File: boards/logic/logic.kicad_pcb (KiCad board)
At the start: 2 copper layers, 49.7 x 57.8 mm, 45 parts, among them IC1 ATTINY85-S, P1 5V_IN, P2 PROG_CONN, P3 DSPLY_CONN, Q1 Q_NPN_EBC, Q2 Q_NPN_EBC, Q3 Q_NPN_EBC, Q4 Q_NPN_EBC, Q5 Q_NPN_EBC, Q6 Q_NPN_EBC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

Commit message: Route ESP8266 ground, and add top and bottom ground planes.
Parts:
- moved G1 1.30 mm to (137.2, 115.7)
- moved G2 1.22 mm to (137.5, 119.3)
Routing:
- net GND: track 13.5 -> 21.9 mm, vias 1 -> 2
- added copper zone on B.Cu, net GND
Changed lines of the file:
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@@
   (general
     (links 117)
-    (no_connects 30)
-    (area 97.104287 47.403566 203.751257 163.830001)
+    (no_connects 16)
+    (area 120.574999 88.824999 170.382001 146.760001)
     (thickness 1.6)
     (drawings 32)
-    (tracks 457)
+    (tracks 462)
     (zones 0)
     (modules 45)
@@
     (34 B.Paste user)
     (35 F.Paste user)
-    (36 B.SilkS user hide)
-    (37 F.SilkS user hide)
+    (36 B.SilkS user)
+    (37 F.SilkS user)
     (38 B.Mask user)
     (39 F.Mask user)
@@
   )
   (module te_logos:te_22mm_width (layer B.Cu)
-    (at 137.414 116.967 180)
+    (at 137.16 115.697 180)
     (fp_text reference G1 (at 0 0 180) (layer B.SilkS) hide
       (effects (font (thickness 0.3)) (justify mirror))
@@
   )
   (module te_logos:te_text_22mm_width (layer B.Cu)
-    (at 137.5156 120.4722 180)
+    (at 137.5156 119.253 180)
     (fp_text reference G2 (at 0 0 180) (layer B.SilkS) hide
       (effects (font (thickness 0.3)) (justify mirror))
@@
   (segment (start 159.385 126.111) (end 156.464 123.19) (width 0.25) (layer F.Cu) (net 1))
   (segment (start 156.464 123.19) (end 131.58324 123.19) (width 0.25) (layer F.Cu) (net 1))
+  (segment (start 167.259 108.077) (end 166.7618 108.077) (width 0.5) (layer B.Cu) (net 2))
+  (segment (start 166.7618 108.077) (end 164.0948 110.744) (width 0.5) (layer B.Cu) (net 2))
+  (segment (start 167.792 104.14) (end 167.792 107.544) (width 0.5) (layer F.Cu) (net 2))
+  (via (at 167.259 108.077) (size 0.6) (drill 0.4) (layers F.Cu B.Cu) (net 2))
+  (segment (start 167.792 107.544) (end 167.259 108.077) (width 0.5) (layer F.Cu) (net 2))
   (segment (start 126.111 139.827) (end 126.111 135.215) (width 0.5) (layer B.Cu) (net 2))
   (segment (start 126.111 135.215) (end 127.468 133.858) (width 0.5) (layer B.Cu) (net 2))
@@
       )
     )
+  )
+  (zone (net 2) (net_name GND) (layer B.Cu) (hatch edge 0.508)
+    (connect_pads (clearance 0.508))
+    (min_thickness 0.254)
+    (fill yes (arc_segments 16) (thermal_gap 0.508) (thermal_bridge_width 0.508))
+    (polygon
+      (pts
+        (xy 170.18 90.297) (xy 169.799 89.535) (xy 169.037 89.154) (xy 121.92 89.154) (xy 121.158 89.408)
+        (xy 120.777 90.043) (xy 120.777 145.415) (xy 121.158 146.177) (xy 121.92 146.558) (xy 169.164 146.558)
+        (xy 169.799 146.177) (xy 170.18 145.542)
+      )
+    )

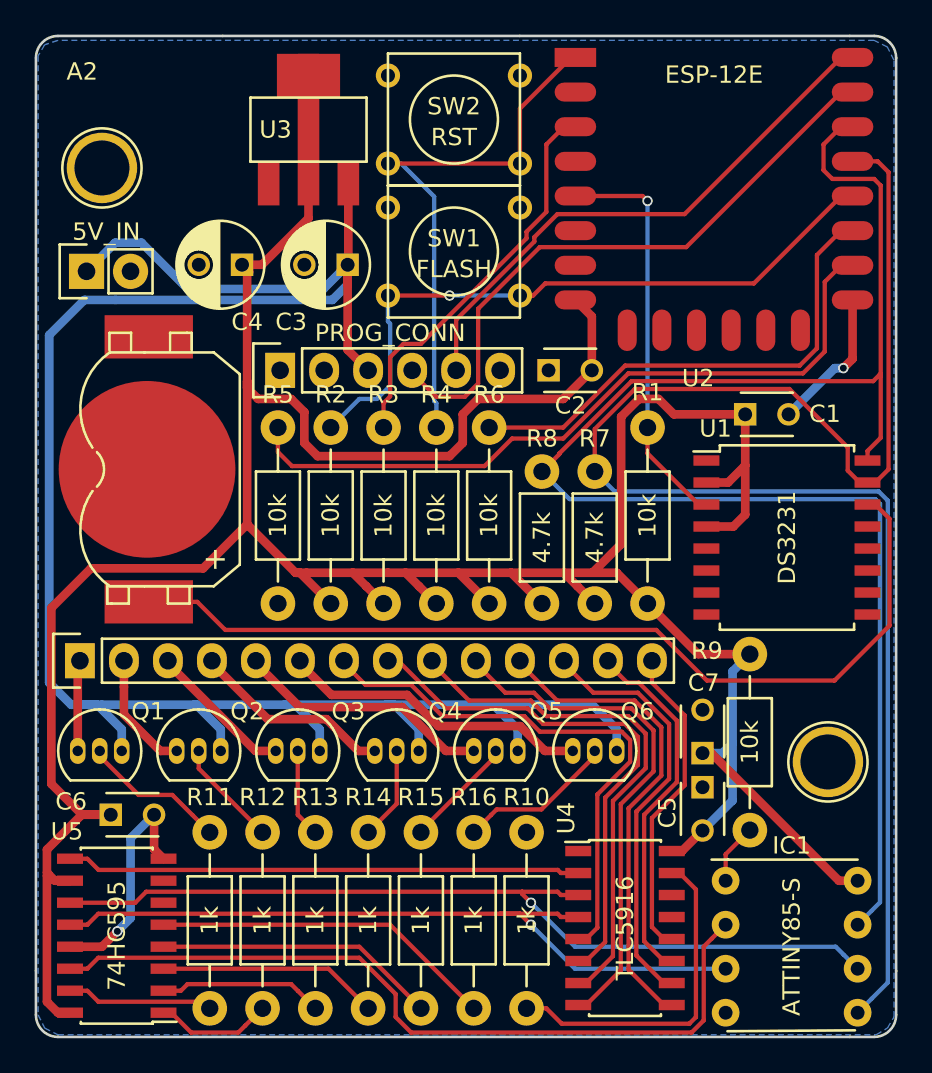
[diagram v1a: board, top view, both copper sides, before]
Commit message: Fix an unconnected ground on the TLC5916 and update the schematic date.
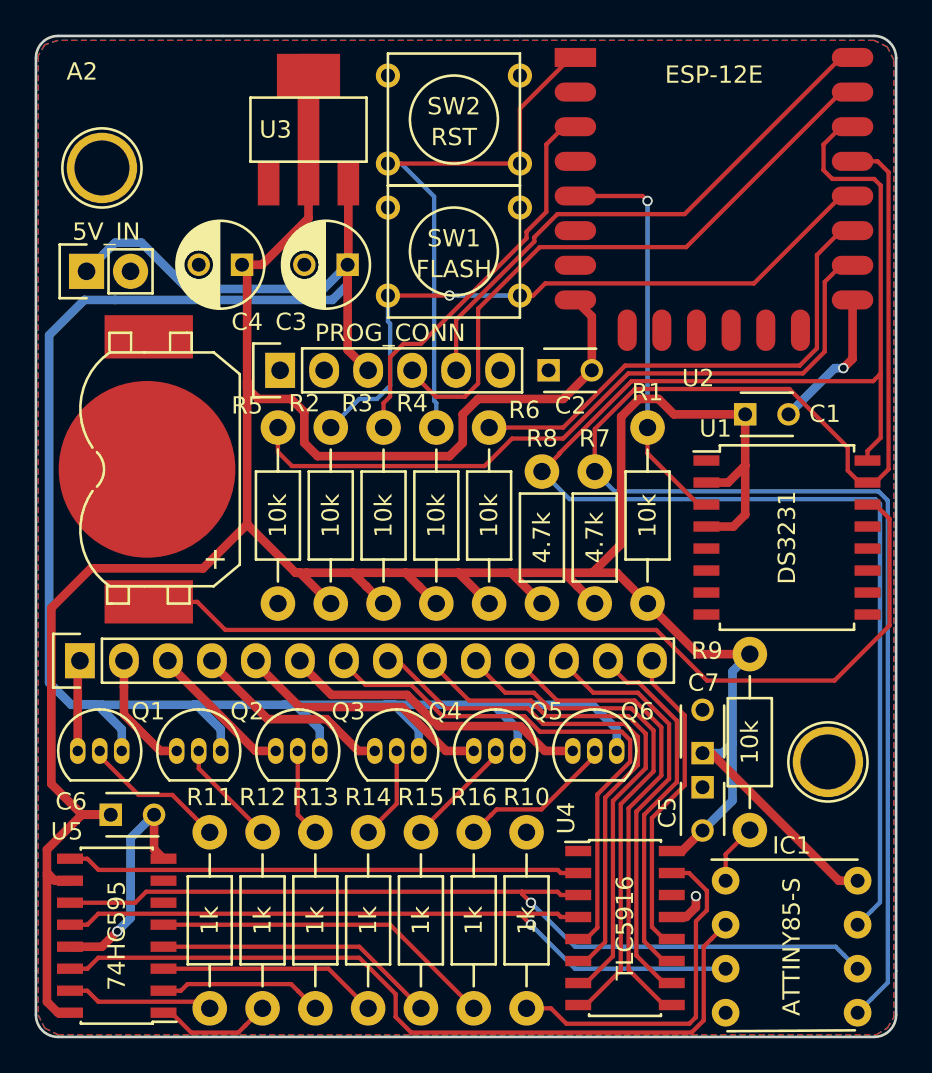
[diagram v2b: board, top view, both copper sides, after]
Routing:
- net GND: track 21.9 -> 24.2 mm, vias 2 -> 3
- net Net-(R10-Pad1): track 19.5 -> 20.3 mm
- added copper zone on F.Cu, net GND
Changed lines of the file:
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@@
   (general
     (links 117)
-    (no_connects 16)
+    (no_connects 1)
     (area 120.574999 88.824999 170.382001 146.760001)
     (thickness 1.6)
     (drawings 32)
-    (tracks 462)
+    (tracks 468)
     (zones 0)
     (modules 45)
@@
     (0 F.Cu signal)
     (31 B.Cu signal)
-    (32 B.Adhes user)
-    (33 F.Adhes user)
-    (34 B.Paste user)
-    (35 F.Paste user)
-    (36 B.SilkS user)
+    (32 B.Adhes user hide)
+    (33 F.Adhes user hide)
+    (34 B.Paste user hide)
+    (35 F.Paste user hide)
+    (36 B.SilkS user hide)
     (37 F.SilkS user)
     (38 B.Mask user)
     (39 F.Mask user)
-    (40 Dwgs.User user)
-    (41 Cmts.User user)
-    (42 Eco1.User user)
-    (43 Eco2.User user)
+    (40 Dwgs.User user hide)
+    (41 Cmts.User user hide)
+    (42 Eco1.User user hide)
+    (43 Eco2.User user hide)
     (44 Edge.Cuts user)
     (45 Margin user)
@@
     (47 F.CrtYd user)
     (48 B.Fab user)
-    (49 F.Fab user)
+    (49 F.Fab user hide)
   )
   (setup
@@
     (descr "Resistor, Axial,  RM 10mm, 1/3W")
     (tags "Resistor Axial RM 10mm 1/3W")
-    (fp_text reference R2 (at 12.065 0 180) (layer F.SilkS)
+    (fp_text reference R2 (at 11.557 -1.524 180) (layer F.SilkS)
       (effects (font (size 1 1) (thickness 0.15)))
     )
@@
     (descr "Resistor, Axial,  RM 10mm, 1/3W")
     (tags "Resistor Axial RM 10mm 1/3W")
-    (fp_text reference R3 (at -1.905 0 360) (layer F.SilkS)
+    (fp_text reference R3 (at -1.397 1.524 360) (layer F.SilkS)
       (effects (font (size 1 1) (thickness 0.15)))
     )
@@
     (descr "Resistor, Axial,  RM 10mm, 1/3W")
     (tags "Resistor Axial RM 10mm 1/3W")
-    (fp_text reference R4 (at 12.065 0 180) (layer F.SilkS)
+    (fp_text reference R4 (at 11.557 -1.397 180) (layer F.SilkS)
       (effects (font (size 1 1) (thickness 0.15)))
     )
@@
     (descr "Resistor, Axial,  RM 10mm, 1/3W")
     (tags "Resistor Axial RM 10mm 1/3W")
-    (fp_text reference R5 (at 12.065 0 180) (layer F.SilkS)
+    (fp_text reference R5 (at 11.43 -1.778 180) (layer F.SilkS)
       (effects (font (size 1 1) (thickness 0.15)))
     )
@@
     (descr "Resistor, Axial,  RM 10mm, 1/3W")
     (tags "Resistor Axial RM 10mm 1/3W")
-    (fp_text reference R6 (at 12.065 0 180) (layer F.SilkS)
+    (fp_text reference R6 (at 11.176 2.032 180) (layer F.SilkS)
       (effects (font (size 1 1) (thickness 0.15)))
     )
@@
   (segment (start 159.385 126.111) (end 156.464 123.19) (width 0.25) (layer F.Cu) (net 1))
   (segment (start 156.464 123.19) (end 131.58324 123.19) (width 0.25) (layer F.Cu) (net 1))
+  (segment (start 157.3555 139.7635) (end 158.1785 139.7635) (width 0.5) (layer F.Cu) (net 2))
+  (segment (start 158.1785 139.7635) (end 158.749994 139.192006) (width 0.5) (layer F.Cu) (net 2))
+  (segment (start 158.749994 139.192006) (end 158.749994 138.557) (width 0.5) (layer F.Cu) (net 2))
+  (via (at 158.749994 138.557) (size 0.6) (drill 0.4) (layers F.Cu B.Cu) (net 2))
   (segment (start 167.259 108.077) (end 166.7618 108.077) (width 0.5) (layer B.Cu) (net 2))
   (segment (start 166.7618 108.077) (end 164.0948 110.744) (width 0.5) (layer B.Cu) (net 2))
@@
   (segment (start 146.812 111.506) (end 151.088331 111.506) (width 0.25) (layer F.Cu) (net 40))
   (segment (start 154.664375 107.929956) (end 164.739044 107.929956) (width 0.25) (layer F.Cu) (net 40))
-  (segment (start 157.3555 137.2235) (end 157.8055 137.2235) (width 0.25) (layer F.Cu) (net 41))
-  (segment (start 157.8055 137.2235) (end 158.75 138.168) (width 0.25) (layer F.Cu) (net 41))
-  (segment (start 158.75 138.168) (end 158.75 145.542) (width 0.25) (layer F.Cu) (net 41))
+  (segment (start 157.3555 137.2235) (end 158.3555 137.2235) (width 0.25) (layer F.Cu) (net 41))
+  (segment (start 158.3555 137.2235) (end 159.385 138.253) (width 0.25) (layer F.Cu) (net 41))
+  (segment (start 150.384492 145.034) (end 148.971 145.034) (width 0.25) (layer F.Cu) (net 41))
+  (segment (start 159.385 138.253) (end 159.385 139.370188) (width 0.25) (layer F.Cu) (net 41))
+  (segment (start 159.385 139.370188) (end 158.75 140.005188) (width 0.25) (layer F.Cu) (net 41))
+  (segment (start 158.75 140.005188) (end 158.75 145.542) (width 0.25) (layer F.Cu) (net 41))
   (segment (start 158.75 145.542) (end 158.369 145.923) (width 0.25) (layer F.Cu) (net 41))
-  (segment (start 158.369 145.923) (end 151.003 145.923) (width 0.25) (layer F.Cu) (net 41))
-  (segment (start 151.003 145.923) (end 150.114 145.034) (width 0.25) (layer F.Cu) (net 41))
-  (segment (start 150.114 145.034) (end 148.971 145.034) (width 0.25) (layer F.Cu) (net 41))
+  (segment (start 158.369 145.923) (end 151.273492 145.923) (width 0.25) (layer F.Cu) (net 41))
+  (segment (start 151.273492 145.923) (end 150.384492 145.034) (width 0.25) (layer F.Cu) (net 41))
   (segment (start 130.683 145.034) (end 130.302 144.653) (width 0.25) (layer F.Cu) (net 42))
   (segment (start 130.302 144.653) (end 124.251 144.653) (width 0.25) (layer F.Cu) (net 42))
@@
     (min_thickness 0.254)
     (keepout (tracks not_allowed) (vias not_allowed) (copperpour not_allowed))
-    (fill (arc_segments 16) (thermal_gap 0.508) (thermal_bridge_width 0.508))
+    (fill yes (arc_segments 16) (thermal_gap 0.508) (thermal_bridge_width 0.508))
     (polygon
       (pts
@@
     (connect_pads (clearance 0.508))
     (min_thickness 0.254)
+    (fill yes (arc_segments 16) (thermal_gap 0.508) (thermal_bridge_width 0.508))
+    (polygon
+      (pts
+        (xy 170.18 90.297) (xy 169.799 89.535) (xy 169.037 89.154) (xy 121.92 89.154) (xy 121.158 89.408)
+        (xy 120.777 90.043) (xy 120.777 145.415) (xy 121.158 146.177) (xy 121.92 146.558) (xy 169.164 146.558)
+        (xy 169.799 146.177) (xy 170.18 145.542)
+      )
+    )
+  )
+  (zone (net 2) (net_name GND) (layer F.Cu) (hatch edge 0.508)
+    (connect_pads (clearance 0.508))
+    (min_thickness 0.254)
